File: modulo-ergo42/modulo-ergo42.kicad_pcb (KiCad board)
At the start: 2 copper layers, 137.2 x 80 mm, 52 parts, among them J1 AudioJack4_Ground, J2 AudioJack4_Ground, J3 AudioJack4_Ground, J4 AudioJack4_Ground, SW1 SW_Push, SW10 SW_Push, SW11 SW_Push, SW12 SW_Push, SW13 SW_Push, SW14 SW_Push, SW15 SW_Push, SW16 SW_Push, SW17 SW_Push, SW18 SW_Push, SW19 SW_Push, SW2 SW_Push, SW20 SW_Push, SW21 SW_Push, SW22 SW_Push, SW23 SW_Push, SW24 SW_Push, SW25 SW_Push, SW26 SW_Push, SW27 SW_Push, SW28 SW_Push, SW29 SW_DIP_x02, SW3 SW_Push, SW4 SW_Push, SW5 SW_Push, SW6 SW_Push, SW7 SW_Push, SW8 SW_Push, SW9 SW_Push, U1 TCA9555PWR, U2 TCA9555PWR

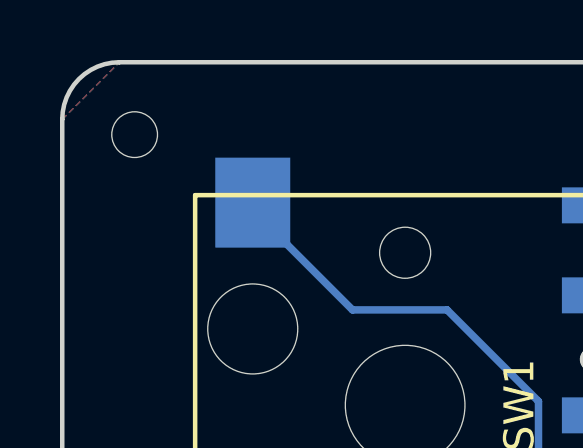
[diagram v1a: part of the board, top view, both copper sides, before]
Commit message: Fix screw hole
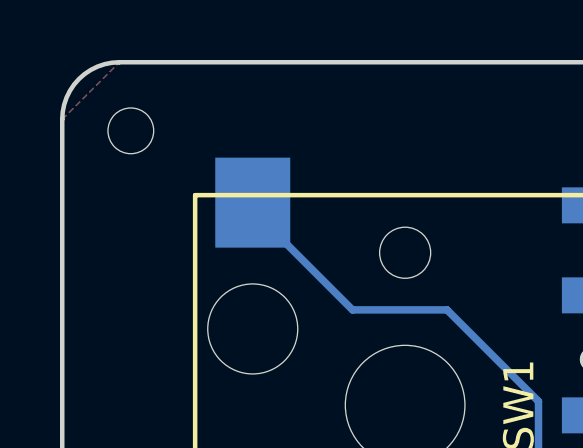
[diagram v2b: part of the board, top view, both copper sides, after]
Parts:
- moved ? 0.18 mm to (56.9, 36.6)
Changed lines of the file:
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@@
   )
   (module library:Screw_Hole (layer F.Cu)
-    (at 57.023 36.703)
+    (at 56.896 36.576)
     (fp_text reference "" (at 0 1.905) (layer F.SilkS)
       (effects (font (size 1 1) (thickness 0.15)))

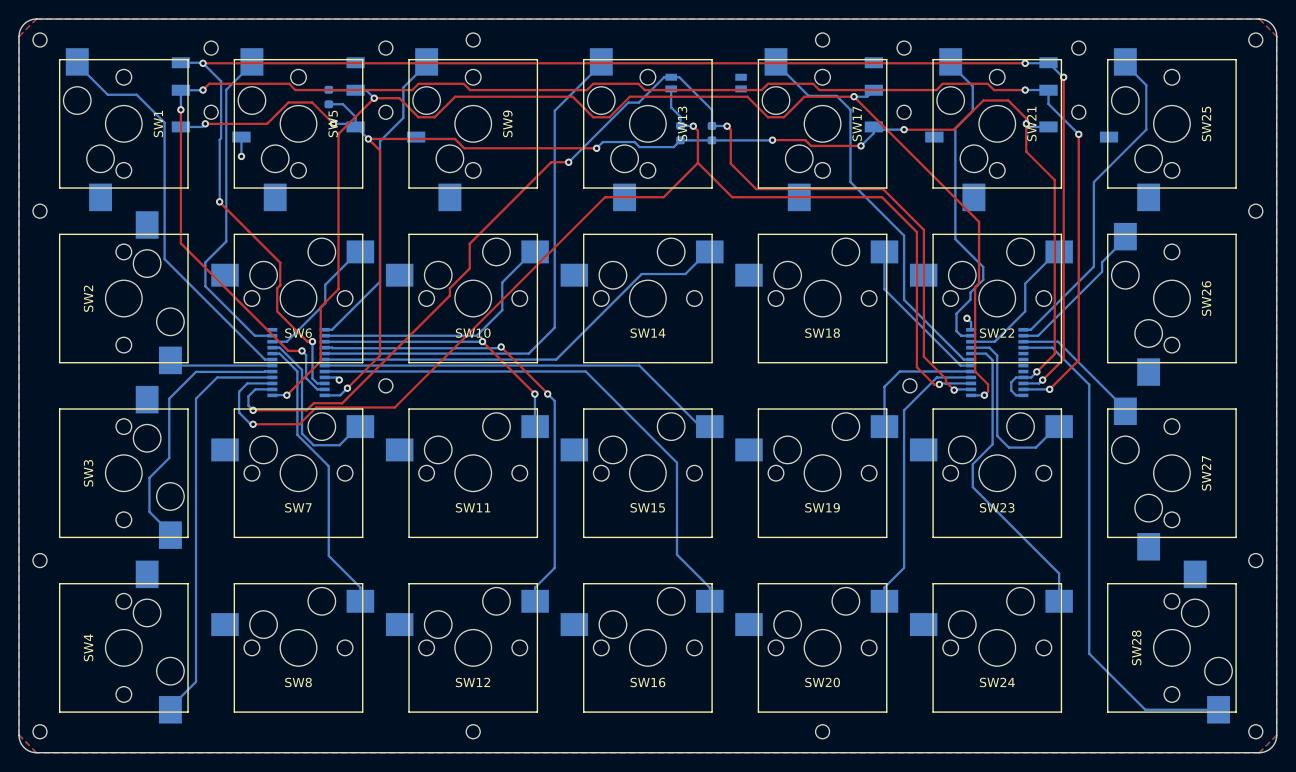
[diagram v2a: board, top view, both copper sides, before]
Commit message: Fix screw hole
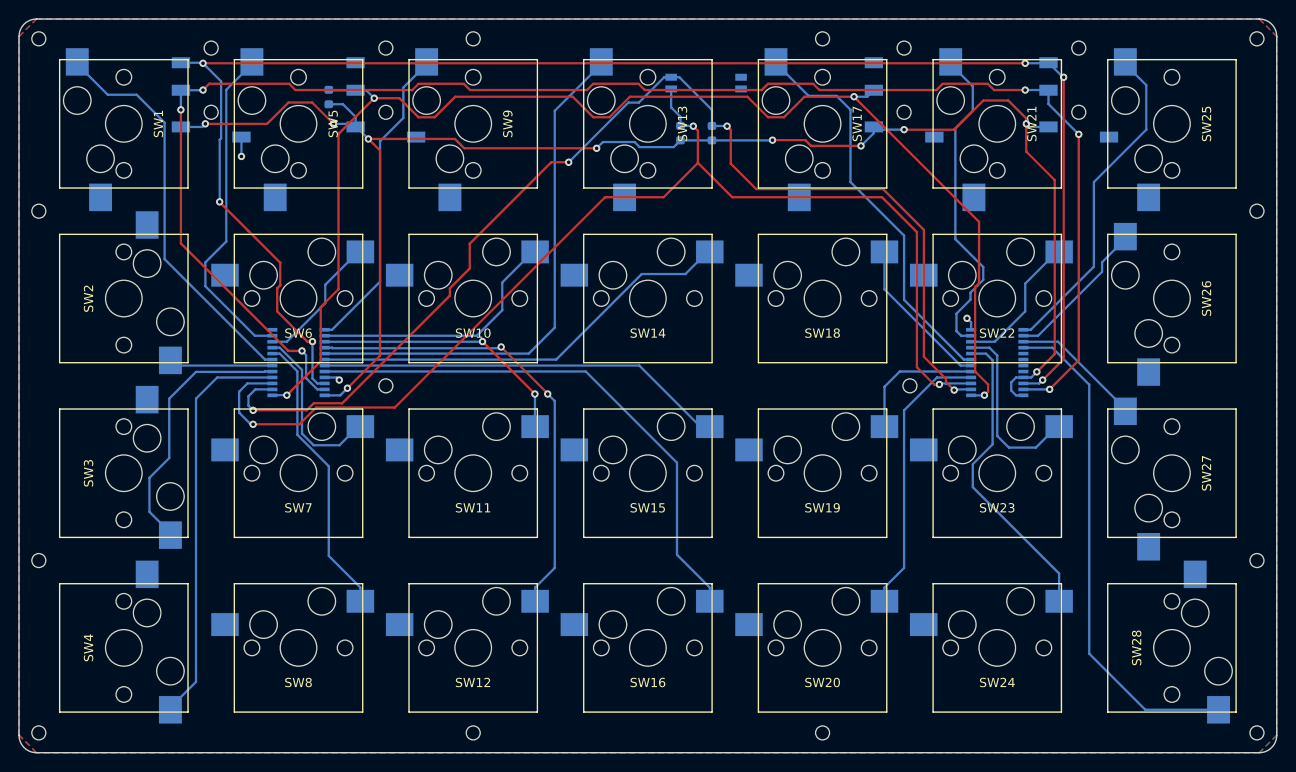
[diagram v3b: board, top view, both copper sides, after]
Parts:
- removed the ? at (56.9, 55.2)
- removed the ? at (142.2, 112.0)
- removed the ? at (189.5, 112.0)
- removed the ? at (189.5, 36.6)
- removed the ? at (56.9, 93.3)
- removed the ? at (189.5, 93.3)
- removed the ? at (189.5, 55.2)
- removed the ? at (142.2, 36.6)
- removed the ? at (56.9, 36.6)
- removed the ? at (56.9, 112.0)
- removed the ? at (104.1, 112.0)
- added ?: Screw_Hole, library:Screw_Hole, F.Cu at (56.8, 55.2)
- added ?: Screw_Hole, library:Screw_Hole, F.Cu at (142.2, 112.1)
- added ?: Screw_Hole, library:Screw_Hole, F.Cu at (189.6, 112.1)
- added ?: Screw_Hole, library:Screw_Hole, F.Cu at (189.6, 36.4)
- added ?: Screw_Hole, library:Screw_Hole, F.Cu at (56.8, 93.3)
- added ?: Screw_Hole, library:Screw_Hole, F.Cu at (189.6, 93.3)
- added ?: Screw_Hole, library:Screw_Hole, F.Cu at (189.6, 55.2)
- added ?: Screw_Hole, library:Screw_Hole, F.Cu at (142.2, 36.4)
- added ?: Screw_Hole, library:Screw_Hole, F.Cu at (56.8, 36.4)
- added ?: Screw_Hole, library:Screw_Hole, F.Cu at (56.8, 112.1)
- added ?: Screw_Hole, library:Screw_Hole, F.Cu at (104.1, 112.1)
- moved ? 0.13 mm to (104.1, 36.4)
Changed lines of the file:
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@@
   )
   (module library:Screw_Hole (layer F.Cu)
-    (at 56.896 55.245)
+    (at 56.769 55.245)
     (fp_text reference "" (at 0 1.905) (layer F.SilkS)
       (effects (font (size 1 1) (thickness 0.15)))
@@
   )
   (module library:Screw_Hole (layer F.Cu)
-    (at 56.896 93.345)
+    (at 56.769 93.345)
     (fp_text reference "" (at 0 1.905) (layer F.SilkS)
       (effects (font (size 1 1) (thickness 0.15)))
@@
   )
   (module library:Screw_Hole (layer F.Cu)
-    (at 189.484 93.345)
+    (at 189.611 93.345)
     (fp_text reference "" (at 0 1.905) (layer F.SilkS)
       (effects (font (size 1 1) (thickness 0.15)))
@@
   )
   (module library:Screw_Hole (layer F.Cu)
-    (at 189.484 55.245)
+    (at 189.611 55.245)
     (fp_text reference "" (at 0 1.905) (layer F.SilkS)
       (effects (font (size 1 1) (thickness 0.15)))
@@
   )
   (module library:Screw_Hole (layer F.Cu)
-    (at 142.24 36.576)
+    (at 142.24 36.449)
     (fp_text reference "" (at 0 1.905) (layer F.SilkS)
       (effects (font (size 1 1) (thickness 0.15)))
@@
   )
   (module library:Screw_Hole (layer F.Cu)
-    (at 104.14 36.576)
+    (at 104.14 36.449)
     (fp_text reference "" (at 0 1.905) (layer F.SilkS)
       (effects (font (size 1 1) (thickness 0.15)))
@@
   )
   (module library:Screw_Hole (layer F.Cu)
-    (at 56.896 36.576)
+    (at 56.769 36.449)
     (fp_text reference "" (at 0 1.905) (layer F.SilkS)
       (effects (font (size 1 1) (thickness 0.15)))
@@
   )
   (module library:Screw_Hole (layer F.Cu)
-    (at 56.896 112.014)
+    (at 56.769 112.141)
     (fp_text reference "" (at 0 1.905) (layer F.SilkS)
       (effects (font (size 1 1) (thickness 0.15)))
@@
   )
   (module library:Screw_Hole (layer F.Cu)
-    (at 104.14 112.014)
+    (at 104.14 112.141)
     (fp_text reference "" (at 0 1.905) (layer F.SilkS)
       (effects (font (size 1 1) (thickness 0.15)))
@@
   )
   (module library:Screw_Hole (layer F.Cu)
-    (at 142.24 112.014)
+    (at 142.24 112.141)
     (fp_text reference "" (at 0 1.905) (layer F.SilkS)
       (effects (font (size 1 1) (thickness 0.15)))
@@
   )
   (module library:Screw_Hole (layer F.Cu)
-    (at 189.484 112.014)
+    (at 189.611 112.141)
     (fp_text reference "" (at 0 1.905) (layer F.SilkS)
       (effects (font (size 1 1) (thickness 0.15)))
@@
   )
   (module library:Screw_Hole (layer F.Cu)
-    (at 189.484 36.576)
+    (at 189.611 36.449)
     (fp_text reference "" (at 0 1.905) (layer F.SilkS)
       (effects (font (size 1 1) (thickness 0.15)))

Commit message: Fix TRRS jack
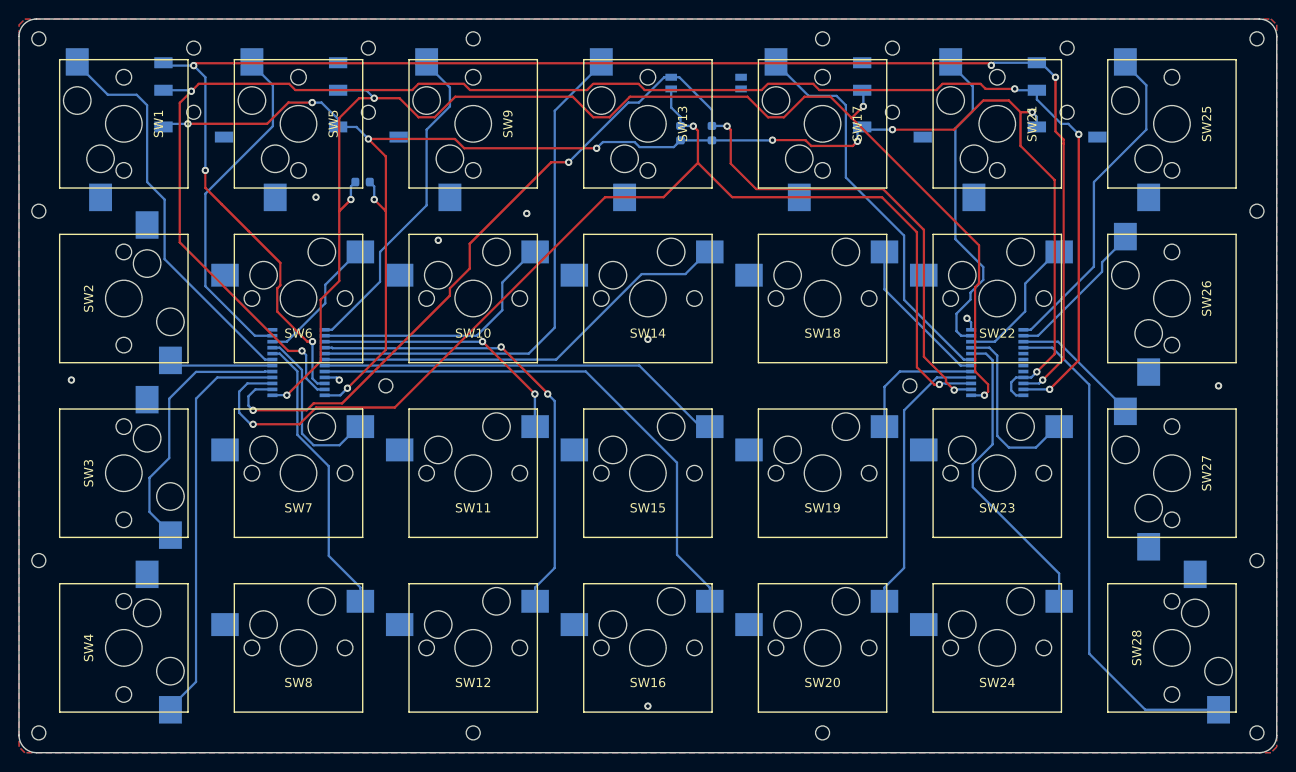
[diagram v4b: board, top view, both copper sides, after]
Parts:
- moved R1 9.98 mm to (92.1, 52.1), turned to 180 degrees
- moved J1 1.91 mm to (73.7, 41.9)
- moved J3 1.91 mm to (92.7, 41.9)
- moved J2 1.27 mm to (168.9, 41.9)
- moved J4 1.27 mm to (149.9, 41.9)
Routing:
- net INT: track 144.1 -> 147.6 mm, vias 4 -> 5
- net 3V3: track 174.5 -> 177.5 mm, vias 10 -> 11
- net SDA: track 176.1 -> 178.2 mm, vias 6 -> 5
- net GND: track 5.27 -> 3.15 mm, vias 3 -> 9
- net R1C3: track 34.3 -> 36.4 mm
- net R1C2: track 36.1 -> 38.0 mm
- net SCL: track 174.8 -> 176.6 mm

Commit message: Implement Beta-1
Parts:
- added C1: 100 p, Capacitor_SMD:C_0603_1608Metric, F.Cu at (123.2, 53.5)
- added C2: 100 p, Capacitor_SMD:C_0603_1608Metric, F.Cu at (123.2, 91.4)
- added C3: 1 u, Capacitor_SMD:C_0603_1608Metric, F.Cu at (73.7, 47.0)
- added C4: 1 u, Capacitor_SMD:C_0603_1608Metric, F.Cu at (168.9, 47.0)
- J1, J2, J3, J4: value AudioJack4_Ground -> AudioJack4
- R1: moved to F.Cu
- R2, R3: value 10 kΩ -> 1 M; moved to F.Cu
- moved U2 42.6 mm to (123.2, 90.8), turned to 270 degrees
- moved U1 42.6 mm to (123.2, 52.7), turned to 270 degrees
- moved SW29 24.1 mm to (109.9, 55.2), turned to 90 degrees
- moved R1 21.7 mm to (113.7, 49.5), turned to 0 degrees
- moved R2 21.6 mm to (109.9, 54.0), turned to 0 degrees
- moved R3 19.5 mm to (109.9, 56.5), turned to 0 degrees
- turned SW13 to 0 degrees
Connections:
- J1 pad R1: SDA -> SCL
- J1 pad R2: SCL -> SDA
- J2 pad R1: SDA -> SCL
- J2 pad R2: SCL -> SDA
- U1 pad 10: R2C2 -> R1C7
- U1 pad 11: R1C2 -> Net-(U1-Pad11)
- U1 pad 13: R1C3 -> R2C7
- U1 pad 14: R2C3 -> R2C6
- U1 pad 15: R3C3 -> R2C5
- U1 pad 16: R4C3 -> R2C4
- U1 pad 17: R1C4 -> R2C3
- U1 pad 18: R2C4 -> R2C2
- U1 pad 19: R3C4 -> R2C1
- U1 pad 20: R4C4 -> Net-(U1-Pad20)
- U1 pad 4: R4C1 -> R1C1
- U1 pad 5: R3C1 -> R1C2
- U1 pad 6: R2C1 -> R1C3
- U1 pad 7: R1C1 -> R1C4
- U1 pad 8: R4C2 -> R1C5
- U1 pad 9: R3C2 -> R1C6
- U2 pad 10: R2C6 -> R3C7
- U2 pad 11: R1C6 -> Net-(U2-Pad11)
- U2 pad 13: R1C7 -> R4C7
- U2 pad 14: R2C7 -> R4C6
- U2 pad 15: R3C7 -> R4C5
- U2 pad 16: R4C7 -> R4C4
- U2 pad 17: Net-(U2-Pad17) -> R4C3
- U2 pad 18: Net-(U2-Pad18) -> R4C2
- U2 pad 19: Net-(U2-Pad19) -> R4C1
- U2 pad 4: R4C5 -> R3C1
- U2 pad 5: R3C5 -> R3C2
- U2 pad 6: R2C5 -> R3C3
- U2 pad 7: R1C5 -> R3C4
- U2 pad 8: R4C6 -> R3C5
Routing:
- net A2: track 127.2 -> 57.0 mm, vias 3 -> 4
- net A1: track 125.7 -> 55.7 mm
- net R2C1: track 11.4 -> 63.5 mm
- net R4C4: track 59.1 -> 6.95 mm
- net R1C4: track 57.3 -> 11.7 mm
- net R3C7: track 14.4 -> 54.9 mm
- net R2C4: track 46.9 -> 6.95 mm
- net INT: track 147.6 -> 109.1 mm, vias 5 -> 4
- net R4C3: track 50.4 -> 16.0 mm, vias 2 -> 0
- net R2C7: track 16.4 -> 50.5 mm
- net R3C4: track 44.8 -> 11.7 mm
- net R3C6: track 20.2 -> 51.1 mm
- net R2C6: track 15.4 -> 43.8 mm
- net R1C1: track 43.6 -> 69.7 mm
- net R1C5: track 43.8 -> 17.8 mm
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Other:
- net class Power added: clearance 0.2, trace_width 0.5, via_dia 0.8, via_drill 0.4

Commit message: Fix some label
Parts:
- C1, C2: value 100 p -> 100 nF
- C3, C4: value 1 u -> 1 uF
- R2, R3: value 1 M -> 1 MΩ
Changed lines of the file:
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@@
       (effects (font (size 1 1) (thickness 0.15)))
     )
-    (fp_text value "1 u" (at 0 1.43 270) (layer F.Fab)
+    (fp_text value "1 uF" (at 0 1.43 270) (layer F.Fab)
       (effects (font (size 1 1) (thickness 0.15)))
     )
@@
       (effects (font (size 1 1) (thickness 0.15)))
     )
-    (fp_text value "100 p" (at 0 1.43) (layer F.Fab)
+    (fp_text value "100 nF" (at 0 1.43) (layer F.Fab)
       (effects (font (size 1 1) (thickness 0.15)))
     )
@@
       (effects (font (size 1 1) (thickness 0.15)))
     )
-    (fp_text value "100 p" (at 0 1.43) (layer F.Fab)
+    (fp_text value "100 nF" (at 0 1.43) (layer F.Fab)
       (effects (font (size 1 1) (thickness 0.15)))
     )
@@
       (effects (font (size 1 1) (thickness 0.15)))
     )
-    (fp_text value "1 M" (at 0 1.43) (layer F.Fab)
+    (fp_text value "1 MΩ" (at 0 1.43) (layer F.Fab)
       (effects (font (size 1 1) (thickness 0.15)))
     )
@@
       (effects (font (size 1 1) (thickness 0.15)))
     )
-    (fp_text value "1 M" (at 0 1.43) (layer F.Fab)
+    (fp_text value "1 MΩ" (at 0 1.43) (layer F.Fab)
       (effects (font (size 1 1) (thickness 0.15)))
     )
@@
       (effects (font (size 1 1) (thickness 0.15)))
     )
-    (fp_text value "1 u" (at 0 1.43 270) (layer F.Fab)
-      (effects (font (size 1 1) (thickness 0.15)))
-    )
+    (fp_text value "1 uF" (at 0 1.43 270) (layer F.Fab)
+      (effects (font (size 1 1) (thickness 0.15)))
+    )
